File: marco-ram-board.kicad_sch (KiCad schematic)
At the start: 0 parts

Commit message: Final annotate pass
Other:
- sheet mcu ports: added BTN, LED; removed none
- sheet mcu-if ports: added BTN, LED; removed none

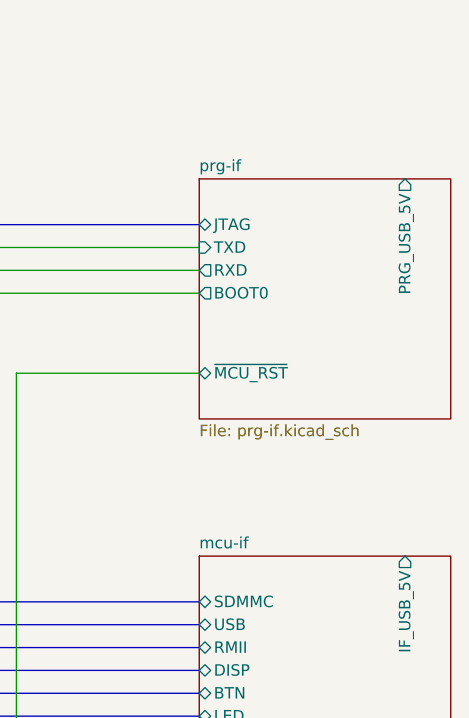
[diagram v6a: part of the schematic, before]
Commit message: Also connect MCU USB VBUS and ID.
Useful for detecting disconnections.
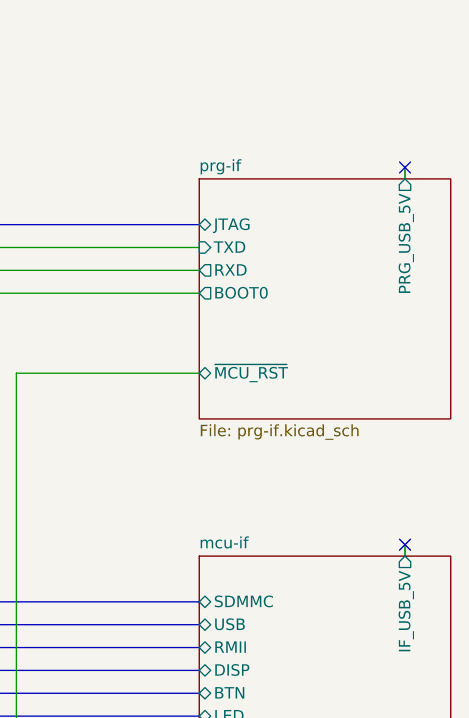
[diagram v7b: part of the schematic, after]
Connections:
- no-connect marks 0 -> 2
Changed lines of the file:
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@@
 (kicad_sch (version 20211123) (generator eeschema)
   (paper "A4")
+  (no_connect (at 231.14 76.2))
+  (no_connect (at 231.14 118.11))
   (wire (pts (xy 187.96 140.97) (xy 187.96 99.06))
     (stroke (width 0) (type default) (color 0 0 0 0))
@@
     (stroke (width 0) (type default) (color 0 0 0 0))
   )
+  (wire (pts (xy 231.14 118.11) (xy 231.14 119.38))
+    (stroke (width 0) (type default) (color 0 0 0 0))
+  )
   (wire (pts (xy 187.96 140.97) (xy 163.83 140.97))
     (stroke (width 0) (type default) (color 0 0 0 0))
@@
   )
   (wire (pts (xy 163.83 90.17) (xy 208.28 90.17))
+    (stroke (width 0) (type default) (color 0 0 0 0))
+  )
+  (wire (pts (xy 231.14 76.2) (xy 231.14 77.47))
     (stroke (width 0) (type default) (color 0 0 0 0))
   )
@@
       (reference "R525") (unit 1) (value "4.7") (footprint "Resistor_SMD:R_0603_1608Metric_Pad0.98x0.95mm_HandSolder")
     )
+    (path "/ef3f0de9-deea-4baf-8cd2-112c438774cf/36faf224-6d62-4451-a816-f4a91175efd8"
+      (reference "R526") (unit 1) (value "10k") (footprint "")
+    )
     (path "/7c962775-7ac8-4e55-b50e-b888d058fafd/a0730651-6647-4a63-a318-43f3d386b902"
